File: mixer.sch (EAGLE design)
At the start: 21 parts, among them U2 SA602AD8-SOIC

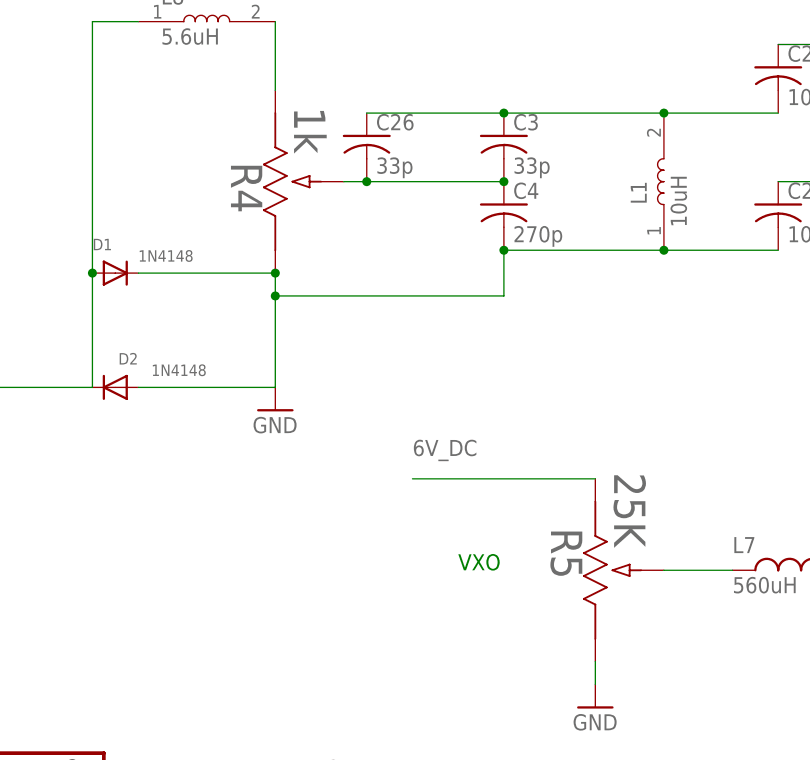
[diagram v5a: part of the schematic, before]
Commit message: Some cleanup
* mixer board had incorrect Resistor labels
* updated schematic PNG
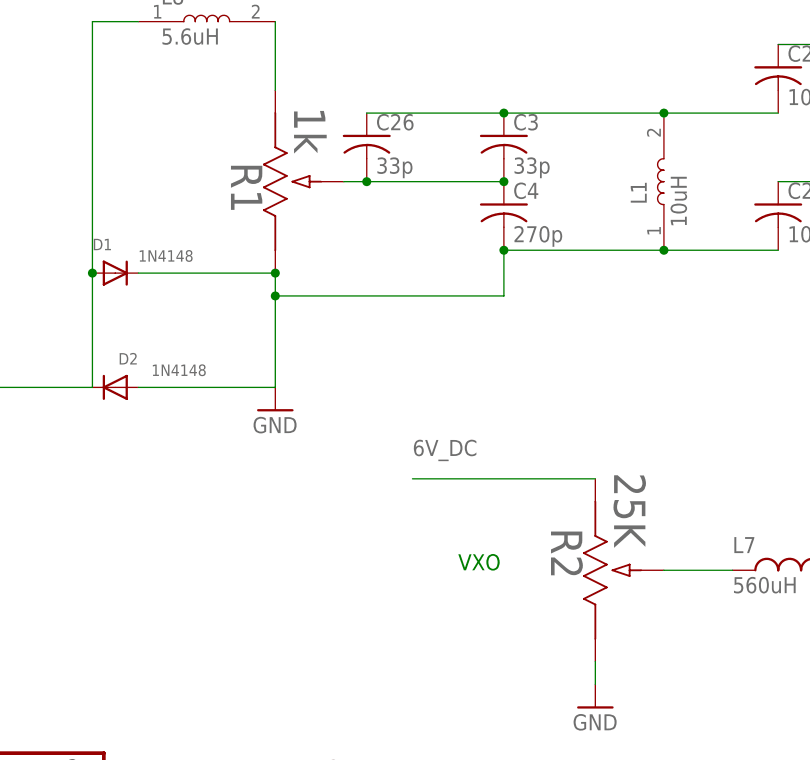
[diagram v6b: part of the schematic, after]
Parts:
- renumbered R4 to R1, R5 to R2
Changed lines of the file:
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@@
 <part name="GND14" library="supply1" library_urn="urn:adsk.eagle:library:371" deviceset="GND" device=""/>
 <part name="JP1" library="adafruit" library_urn="urn:adsk.eagle:library:420" deviceset="PINHD-2X4" device="" package3d_urn="urn:adsk.eagle:package:6240893/1"/>
-<part name="R4" library="zort2" deviceset="3362W-1-102LF" device="" value="1k"/>
-<part name="R5" library="zort2" deviceset="3362W-1-102LF" device="" value="25K"/>
+<part name="R1" library="zort2" deviceset="3362W-1-102LF" device="" value="1k"/>
+<part name="R2" library="zort2" deviceset="3362W-1-102LF" device="" value="25K"/>
 <part name="CRYSTAL" library="adafruit" library_urn="urn:adsk.eagle:library:420" deviceset="PINHD-1X3" device="" package3d_urn="urn:adsk.eagle:package:6240710/1"/>
 </parts>
@@
 <attribute name="VALUE" x="-44.45" y="10.16" size="1.778" layer="96"/>
 </instance>
-<instance part="R4" gate="A" x="-10.16" y="99.06" smashed="yes" rot="R270">
+<instance part="R1" gate="A" x="-10.16" y="99.06" smashed="yes" rot="R270">
 <attribute name="NAME" x="-15.0876" y="91.0844" size="3.4798" layer="95" ratio="10" rot="SR270"/>
 <attribute name="VALUE" x="-8.0772" y="97.2312" size="3.4798" layer="96" ratio="10" rot="SR270"/>
 </instance>
-<instance part="R5" gate="A" x="25.4" y="55.88" smashed="yes" rot="R270">
+<instance part="R2" gate="A" x="25.4" y="55.88" smashed="yes" rot="R270">
 <attribute name="NAME" x="20.4724" y="50.4444" size="3.4798" layer="95" ratio="10" rot="SR270"/>
 <attribute name="VALUE" x="27.4828" y="56.5912" size="3.4798" layer="96" ratio="10" rot="SR270"/>
@@
 <wire x1="-25.4" y1="78.74" x2="-10.16" y2="78.74" width="0.1524" layer="91"/>
 <wire x1="-10.16" y1="78.74" x2="-10.16" y2="76.2" width="0.1524" layer="91"/>
-<pinref part="R4" gate="A" pin="3"/>
+<pinref part="R1" gate="A" pin="3"/>
 <junction x="-10.16" y="78.74"/>
 </segment>
@@
 </segment>
 <segment>
-<pinref part="R5" gate="A" pin="3"/>
+<pinref part="R2" gate="A" pin="3"/>
 <pinref part="GND13" gate="1" pin="GND"/>
 <wire x1="25.4" y1="35.56" x2="25.4" y2="33.02" width="0.1524" layer="91"/>
@@
 <wire x1="25.4" y1="55.88" x2="5.08" y2="55.88" width="0.1524" layer="91"/>
 <label x="5.08" y="58.42" size="1.778" layer="95"/>
-<pinref part="R5" gate="A" pin="1"/>
+<pinref part="R2" gate="A" pin="1"/>
 </segment>
 <segment>
@@
 <wire x1="-2.54" y1="88.9" x2="0" y2="88.9" width="0.1524" layer="91"/>
 <junction x="0" y="88.9"/>
-<pinref part="R4" gate="A" pin="2"/>
+<pinref part="R1" gate="A" pin="2"/>
 </segment>
 </net>
@@
 <pinref part="L8" gate="G$1" pin="2"/>
 <wire x1="-10.16" y1="99.06" x2="-10.16" y2="106.68" width="0.1524" layer="91"/>
-<pinref part="R4" gate="A" pin="1"/>
+<pinref part="R1" gate="A" pin="1"/>
 </segment>
 </net>
@@
 <pinref part="L7" gate="G$1" pin="1"/>
 <wire x1="40.64" y1="45.72" x2="33.02" y2="45.72" width="0.1524" layer="91"/>
-<pinref part="R5" gate="A" pin="2"/>
-</segment>
-</net>
+<pinref part="R2" gate="A" pin="2"/>
+</segment>
+</net>

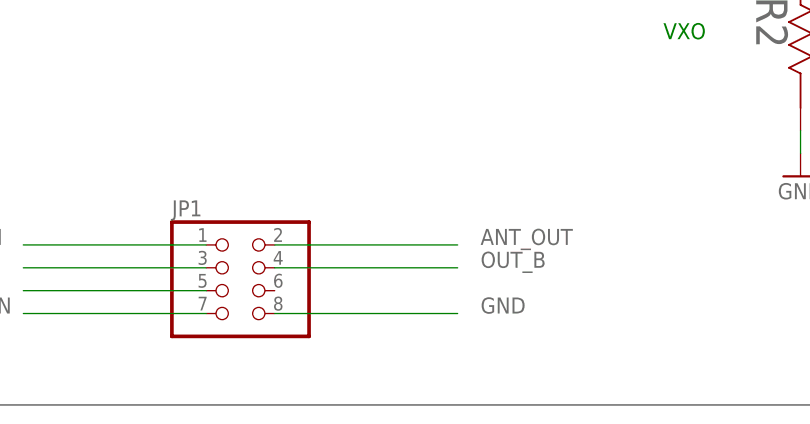
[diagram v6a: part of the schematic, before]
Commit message: v1.2 boards
* corrected C22 as a 33uF (vs 33pF) capacitor with a 1206 footprint
* Q2 emitter is now tied to Q1 emitter and KEY_IN to cut down on self resonance
* Unused pin 4 on JP1 now tied to GND
* All pins on JP1 labelled on top and bottom of each board
* lots more GND vias
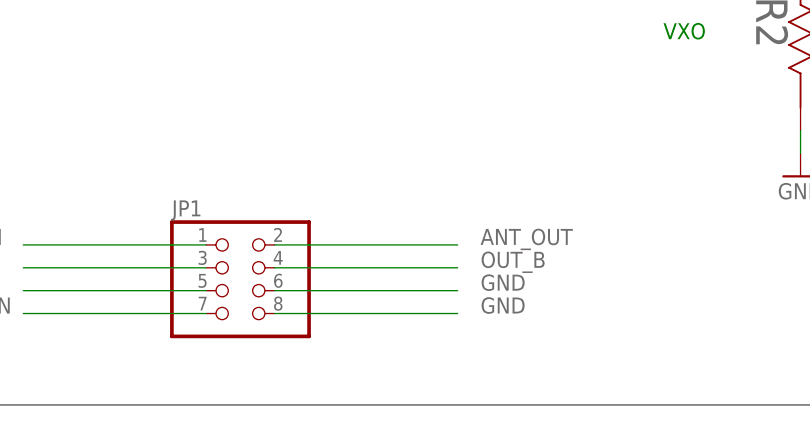
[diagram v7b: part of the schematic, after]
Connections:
- net GND: now also JP1.6
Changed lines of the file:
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@@
 <label x="-10.16" y="15.24" size="1.778" layer="95"/>
+</segment>
+<segment>
+<pinref part="JP1" gate="A" pin="6"/>
+<wire x1="-33.02" y1="17.78" x2="-12.7" y2="17.78" width="0.1524" layer="91"/>
+<label x="-10.16" y="17.78" size="1.778" layer="95"/>
 </segment>
 </net>
